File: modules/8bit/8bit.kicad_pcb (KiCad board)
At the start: 2 copper layers, 30.5 x 68.6 mm, 24 parts, among them SW1 MODE SELECT, U1 MCP6002-xSN, U2 ATtiny1616-M, U3 MCP6002-xSN

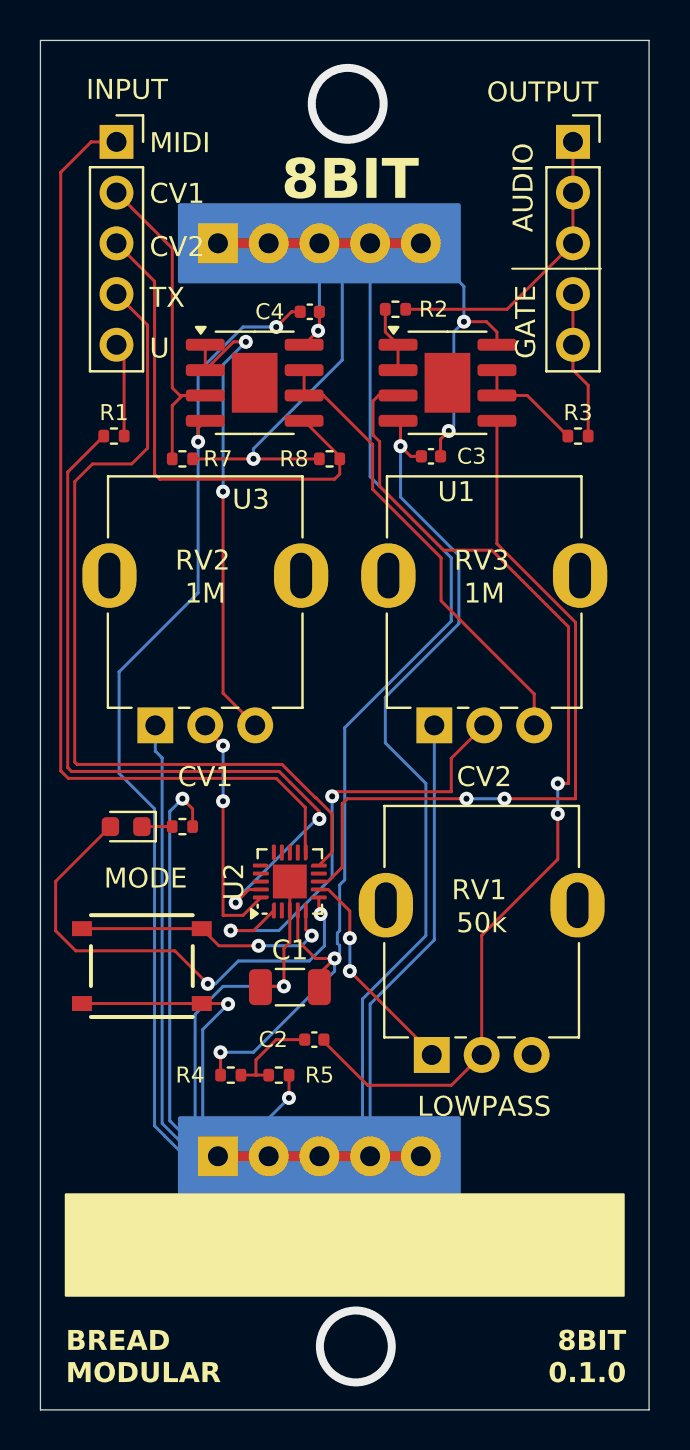
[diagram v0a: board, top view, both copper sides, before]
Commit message: 8bit: Add MIDI THRU support
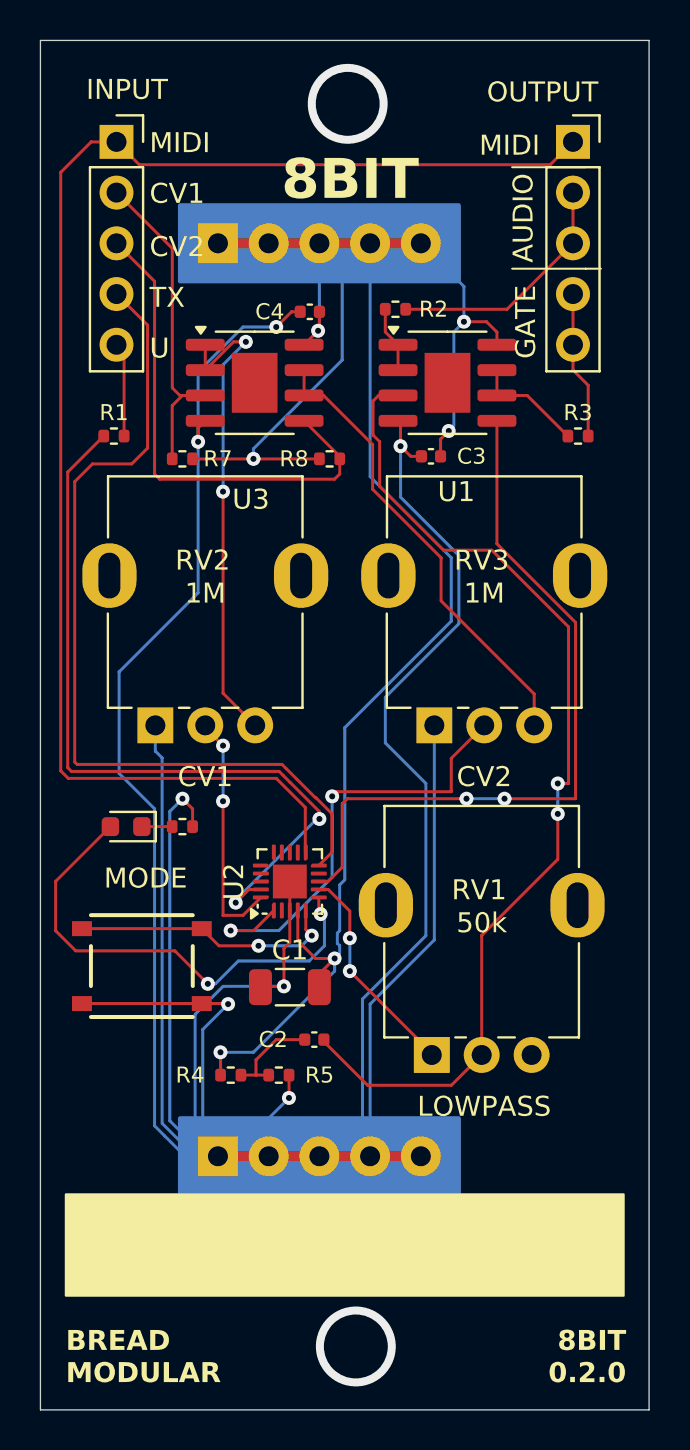
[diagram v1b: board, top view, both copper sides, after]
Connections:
- OUTPUT1 pad 1: AUDIO_OUT -> MIDI
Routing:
- net MIDI: track 48.7 -> 72.5 mm
- net AUDIO_OUT: track 14.8 -> 12.3 mm
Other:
- board text added: "8BIT 0.2.0"
- board text removed: "8BIT 0.1.0"
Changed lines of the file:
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@@
 			(layers "*.Cu" "*.Mask")
 			(remove_unused_layers no)
-			(net 13 "AUDIO_OUT")
+			(net 8 "MIDI")
 			(pinfunction "Pin_1")
 			(pintype "passive")
@@
 		(layer "F.SilkS")
 	)
+	(gr_line
+		(start 70.612 46.99)
+		(end 74.295 46.99)
+		(stroke
+			(width 0.1)
+			(type default)
+		)
+		(layer "F.SilkS")
+	)
 	(gr_poly
 		(pts
@@
 	)
 	(gr_text "AUDIO"
-		(at 71.755 48.006 90)
+		(at 71.755 49.53 90)
 		(layer "F.SilkS")
 		(effects
@@
 		)
 	)
-	(gr_text "8BIT\n0.1.0"
+	(gr_text "MIDI"
+		(at 72.009 46.482 0)
+		(layer "F.SilkS")
+		(effects
+			(font
+				(size 1 1)
+				(thickness 0.15)
+			)
+			(justify right bottom)
+		)
+	)
+	(gr_text "8BIT\n0.2.0"
 		(at 76.327 107.95 0)
 		(layer "F.SilkS")
@@
 	)
 	(segment
+		(start 72.517 46.863)
+		(end 51.943 46.863)
+		(width 0.15)
+		(layer "F.Cu")
+		(net 8)
+	)
+	(segment
 		(start 60.255 81.31)
 		(end 60.28 81.31)
@@
 		(start 49.53 45.72)
 		(end 48.006 47.244)
+		(width 0.15)
+		(layer "F.Cu")
+		(net 8)
+	)
+	(segment
+		(start 73.66 45.72)
+		(end 72.517 46.863)
+		(width 0.15)
+		(layer "F.Cu")
+		(net 8)
+	)
+	(segment
+		(start 51.943 46.863)
+		(end 50.8 45.72)
 		(width 0.15)
 		(layer "F.Cu")
@@
 	)
 	(segment
-		(start 73.66 50.8)
-		(end 73.66 45.72)
-		(width 0.15)
-		(layer "F.Cu")
-		(net 13)
-	)
-	(segment
 		(start 65.28 54.102)
 		(end 70.358 54.102)
@@
 		(width 0.15)
 		(layer "F.Cu")
+		(net 13)
+	)
+	(segment
+		(start 73.66 50.8)
+		(end 73.66 48.26)
+		(width 0.15)
+		(layer "F.Cu")

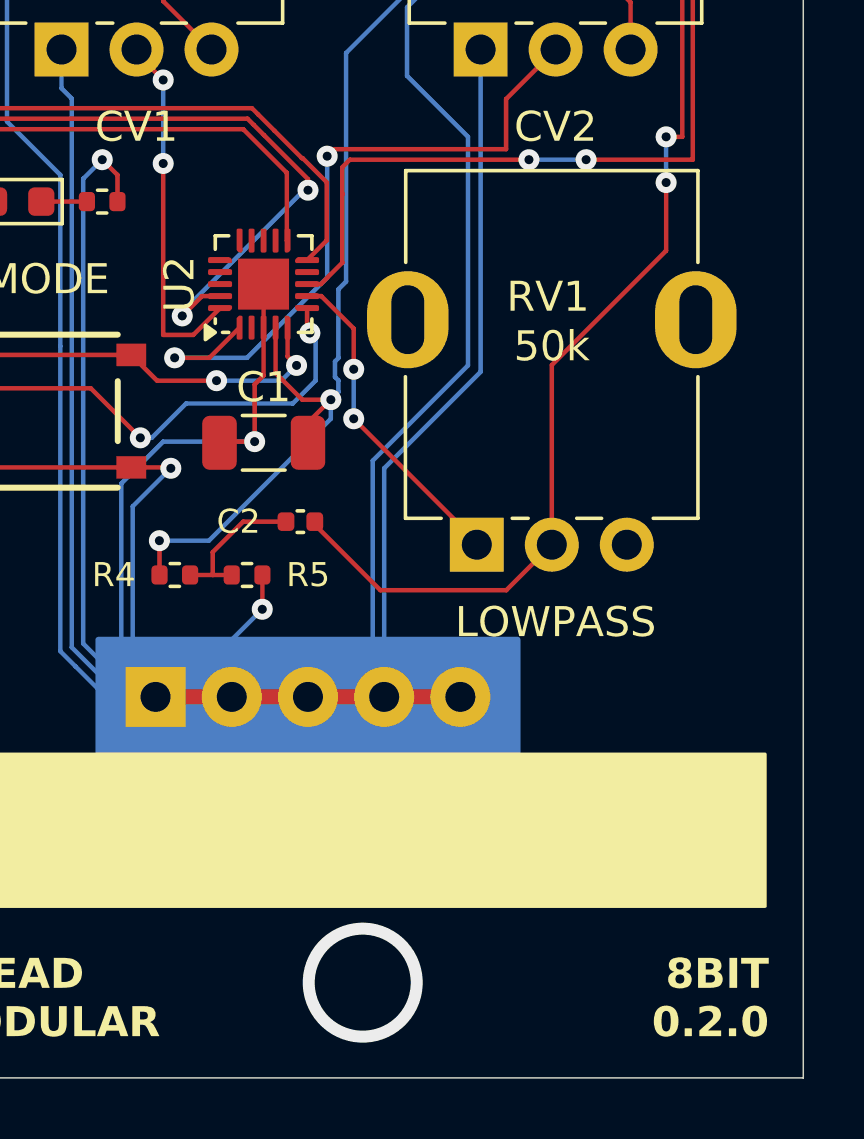
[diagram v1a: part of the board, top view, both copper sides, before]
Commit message: 8bit: Use PB2 as the serial port We used a Software Serial earlier and it uses some memory and flash where we could use somewhere else. Now we go back to the Serial port.
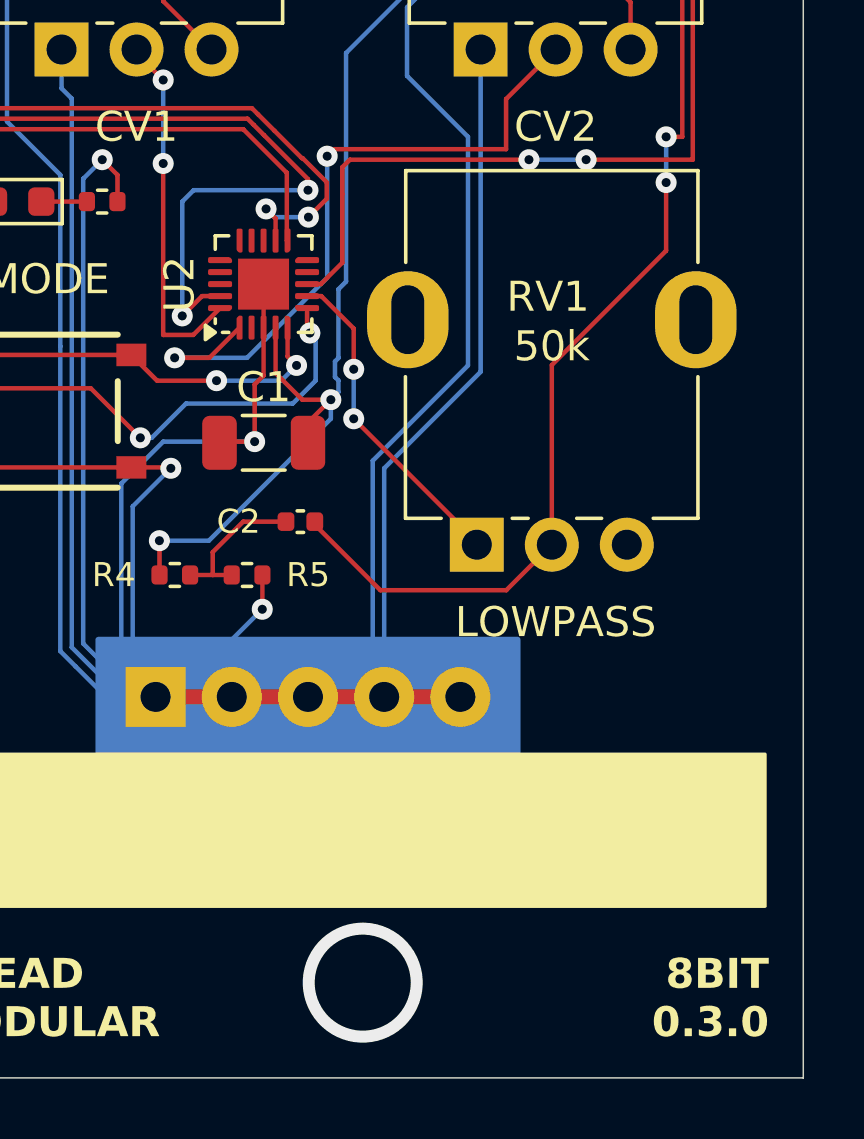
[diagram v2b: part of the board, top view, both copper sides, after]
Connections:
- U2 pad 10: TX -> unconnected-(U2-PB4-Pad10)
- U2 pad 12: unconnected-(U2-PB2-Pad12) -> TX
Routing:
- net Net-(U2-~{RESET}/PA0): track 38.8 -> 40.9 mm
- net TX: track 43.6 -> 44.8 mm, vias 0 -> 2
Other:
- board text added: "8BIT 0.3.0"
- board text removed: "8BIT 0.2.0"
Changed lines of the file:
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@@
 	(net 26 "unconnected-(U2-PC0-Pad15)")
 	(net 27 "unconnected-(U2-PC3-Pad18)")
-	(net 28 "unconnected-(U2-PB2-Pad12)")
+	(net 28 "unconnected-(U2-PB4-Pad10)")
 	(net 29 "unconnected-(U2-PA3-Pad2)")
 	(net 30 "unconnected-(U2-PB5-Pad9)")
@@
 			(size 0.143431 0.143431)
 			(layers "F.Cu" "F.Paste" "F.Mask")
-			(net 7 "TX")
+			(net 28 "unconnected-(U2-PB4-Pad10)")
 			(pinfunction "PB4")
 			(pintype "bidirectional")
@@
 			(layers "F.Cu" "F.Paste" "F.Mask")
 			(roundrect_rratio 0.25)
-			(net 28 "unconnected-(U2-PB2-Pad12)")
+			(net 7 "TX")
 			(pinfunction "PB2")
 			(pintype "bidirectional")
@@
 		)
 	)
-	(gr_text "8BIT\n0.2.0"
+	(gr_text "8BIT\n0.3.0"
 		(at 76.327 107.95 0)
 		(layer "F.SilkS")
@@
 	)
 	(segment
-		(start 49.595 61.849)
-		(end 51.562 61.849)
+		(start 61.585 79.365)
+		(end 61.585 79.918844)
 		(width 0.15)
 		(layer "F.Cu")
@@
 	)
 	(segment
-		(start 52.355 54.895)
-		(end 50.8 53.34)
+		(start 49.595 61.849)
+		(end 51.562 61.849)
 		(width 0.15)
 		(layer "F.Cu")
@@
 	)
 	(segment
-		(start 60.93 81.96)
-		(end 61.585 81.305)
+		(start 52.355 54.895)
+		(end 50.8 53.34)
 		(width 0.15)
 		(layer "F.Cu")
@@
 	)
 	(segment
-		(start 61.585 81.305)
-		(end 61.585 79.365)
+		(start 59.842988 77.649039)
+		(end 59.295975 77.102025)
 		(width 0.15)
 		(layer "F.Cu")
@@
 	)
 	(segment
-		(start 59.842988 77.649039)
-		(end 59.295975 77.102025)
+		(start 61.585 79.918844)
+		(end 60.974966 80.528878)
 		(width 0.15)
 		(layer "F.Cu")
@@
 	)
 	(segment
+		(start 59.563 80.254)
+		(end 59.88 80.571)
+		(width 0.15)
+		(layer "F.Cu")
+		(net 7)
+	)
+	(segment
 		(start 60.782526 78.562526)
 		(end 60.756474 78.562526)
@@
 	)
 	(segment
+		(start 59.88 80.571)
+		(end 59.88 81.31)
+		(width 0.15)
+		(layer "F.Cu")
+		(net 7)
+	)
+	(via
+		(at 59.563 80.254)
+		(size 0.7)
+		(drill 0.3)
+		(layers "F.Cu" "B.Cu")
+		(net 7)
+	)
+	(via
+		(at 60.974966 80.528878)
+		(size 0.7)
+		(drill 0.3)
+		(layers "F.Cu" "B.Cu")
+		(net 7)
+	)
+	(segment
+		(start 60.974966 80.528878)
+		(end 59.837878 80.528878)
+		(width 0.15)
+		(layer "B.Cu")
+		(net 7)
+	)
+	(segment
+		(start 59.837878 80.528878)
+		(end 59.563 80.254)
+		(width 0.15)
+		(layer "B.Cu")
+		(net 7)
+	)
+	(segment
 		(start 72.517 46.863)
 		(end 51.943 46.863)
@@
 	)
 	(segment
-		(start 60.827884 79.629)
-		(end 60.96 79.629)
+		(start 56.769 83.82)
+		(end 56.769 80.01)
 		(width 0.15)
 		(layer "B.Cu")
@@
 	)
 	(segment
-		(start 56.769 83.82)
-		(end 56.769 83.687884)
+		(start 56.769 80.01)
+		(end 57.15 79.629)
 		(width 0.15)
 		(layer "B.Cu")
@@
 	)
 	(segment
-		(start 56.769 83.687884)
-		(end 60.827884 79.629)
+		(start 57.15 79.629)
+		(end 60.96 79.629)
 		(width 0.15)
 		(layer "B.Cu")

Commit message: 8bit_1.0.0
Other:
- board text added: "8BIT 1.0.0"
- board text removed: "8BIT 0.3.0"
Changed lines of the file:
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@@
 		)
 	)
-	(gr_text "8BIT\n0.3.0"
+	(gr_text "8BIT\n1.0.0"
 		(at 76.327 107.95 0)
 		(layer "F.SilkS")
